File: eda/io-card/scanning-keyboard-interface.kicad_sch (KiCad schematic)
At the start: 17 parts, among them J7 Keyboard connector, U10 74HCT193, U11 74HCT541, U4 NE555P, U5 74HCT00, U8 74HCT138, U9 74HCT148

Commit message: Add expansion backplane
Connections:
- net Scancode0: now also U11.7 (A5); no longer U11.2 (A0)
- net Scancode1: now also U11.6 (A4); no longer U11.3 (A1)
- net Scancode2: now also U11.5 (A3); no longer U11.4 (A2)
- net Scancode3: now also U11.2 (A0); no longer U11.5 (A3)
- net Scancode4: now also U11.3 (A1); no longer U11.6 (A4)
- net Scancode5: now also U11.4 (A2); no longer U11.7 (A5)
- net mod0: now also U11.9 (A7); no longer U11.8 (A6)
- net mod1: now also U11.8 (A6); no longer U11.9 (A7)
- net row4: now also U9.4 (I7); no longer U9.1 (I4)
- net row5: now also U9.3 (I6); no longer U9.2 (I5)
- net row6: now also U9.2 (I5); no longer U9.3 (I6)
- net row7: now also U9.1 (I4); no longer U9.4 (I7)
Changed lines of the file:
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@@
     (stroke (width 0) (type default))
   )
-  (label "KeyboardBit6" (at 248.92 60.96 0)
+  (label "KeyboardBit6" (at 248.92 60.96 0) (fields_autoplaced)
     (effects (font (size 1.27 1.27)) (justify left bottom))
   )
@@
     (effects (font (size 1.27 1.27)) (justify right bottom))
   )
-  (label "row5" (at 113.03 111.76 180) (fields_autoplaced)
+  (label "row5" (at 113.03 114.3 180) (fields_autoplaced)
     (effects (font (size 1.27 1.27)) (justify right bottom))
   )
@@
     (effects (font (size 1.27 1.27)) (justify left bottom))
   )
-  (label "Scancode2" (at 217.17 50.8 180) (fields_autoplaced)
+  (label "Scancode2" (at 217.17 53.34 180) (fields_autoplaced)
     (effects (font (size 1.27 1.27)) (justify right bottom))
   )
-  (label "KeyboardBit1" (at 248.92 48.26 0)
+  (label "KeyboardBit1" (at 248.92 48.26 0) (fields_autoplaced)
     (effects (font (size 1.27 1.27)) (justify left bottom))
   )
@@
     (effects (font (size 1.27 1.27)) (justify left bottom))
   )
-  (label "KeyboardBit2" (at 248.92 50.8 0)
+  (label "KeyboardBit2" (at 248.92 50.8 0) (fields_autoplaced)
     (effects (font (size 1.27 1.27)) (justify left bottom))
   )
@@
     (effects (font (size 1.27 1.27)) (justify right bottom))
   )
-  (label "Scancode5" (at 217.17 58.42 180) (fields_autoplaced)
+  (label "Scancode5" (at 217.17 50.8 180) (fields_autoplaced)
     (effects (font (size 1.27 1.27)) (justify right bottom))
   )
-  (label "row7" (at 113.03 116.84 180) (fields_autoplaced)
+  (label "row7" (at 113.03 109.22 180) (fields_autoplaced)
     (effects (font (size 1.27 1.27)) (justify right bottom))
   )
-  (label "KeyboardBit7" (at 248.92 63.5 0)
+  (label "KeyboardBit7" (at 248.92 63.5 0) (fields_autoplaced)
     (effects (font (size 1.27 1.27)) (justify left bottom))
   )
@@
     (effects (font (size 1.27 1.27)) (justify left bottom))
   )
-  (label "KeyboardBit3" (at 248.92 53.34 0)
+  (label "KeyboardBit3" (at 248.92 53.34 0) (fields_autoplaced)
     (effects (font (size 1.27 1.27)) (justify left bottom))
   )
@@
     (effects (font (size 1.27 1.27)) (justify left bottom))
   )
-  (label "mod1" (at 207.01 63.5 0) (fields_autoplaced)
+  (label "mod1" (at 207.01 60.96 0) (fields_autoplaced)
     (effects (font (size 1.27 1.27)) (justify left bottom))
   )
@@
     (effects (font (size 1.27 1.27)) (justify left bottom))
   )
-  (label "row4" (at 113.03 109.22 180) (fields_autoplaced)
+  (label "row4" (at 113.03 116.84 180) (fields_autoplaced)
     (effects (font (size 1.27 1.27)) (justify right bottom))
   )
@@
     (effects (font (size 1.27 1.27)) (justify left bottom))
   )
-  (label "Scancode1" (at 217.17 48.26 180) (fields_autoplaced)
+  (label "Scancode1" (at 217.17 55.88 180) (fields_autoplaced)
     (effects (font (size 1.27 1.27)) (justify right bottom))
   )
-  (label "Scancode0" (at 217.17 45.72 180) (fields_autoplaced)
+  (label "Scancode0" (at 217.17 58.42 180) (fields_autoplaced)
     (effects (font (size 1.27 1.27)) (justify right bottom))
   )
-  (label "KeyboardBit5" (at 248.92 58.42 0)
+  (label "KeyboardBit5" (at 248.92 58.42 0) (fields_autoplaced)
     (effects (font (size 1.27 1.27)) (justify left bottom))
   )
-  (label "Scancode4" (at 217.17 55.88 180) (fields_autoplaced)
+  (label "Scancode4" (at 217.17 48.26 180) (fields_autoplaced)
     (effects (font (size 1.27 1.27)) (justify right bottom))
   )
@@
     (effects (font (size 1.27 1.27)) (justify right bottom))
   )
-  (label "mod0" (at 207.01 60.96 0) (fields_autoplaced)
+  (label "mod0" (at 207.01 63.5 0) (fields_autoplaced)
     (effects (font (size 1.27 1.27)) (justify left bottom))
   )
@@
     (effects (font (size 1.27 1.27)) (justify left bottom))
   )
-  (label "row6" (at 113.03 114.3 180) (fields_autoplaced)
+  (label "row6" (at 113.03 111.76 180) (fields_autoplaced)
     (effects (font (size 1.27 1.27)) (justify right bottom))
   )
-  (label "Scancode3" (at 217.17 53.34 180) (fields_autoplaced)
+  (label "Scancode3" (at 217.17 45.72 180) (fields_autoplaced)
     (effects (font (size 1.27 1.27)) (justify right bottom))
   )
@@
     (effects (font (size 1.27 1.27)) (justify right bottom))
   )
-  (label "KeyboardBit4" (at 248.92 55.88 0)
+  (label "KeyboardBit4" (at 248.92 55.88 0) (fields_autoplaced)
     (effects (font (size 1.27 1.27)) (justify left bottom))
   )
-  (label "KeyboardBit0" (at 248.92 45.72 0)
+  (label "KeyboardBit0" (at 248.92 45.72 0) (fields_autoplaced)
     (effects (font (size 1.27 1.27)) (justify left bottom))
   )

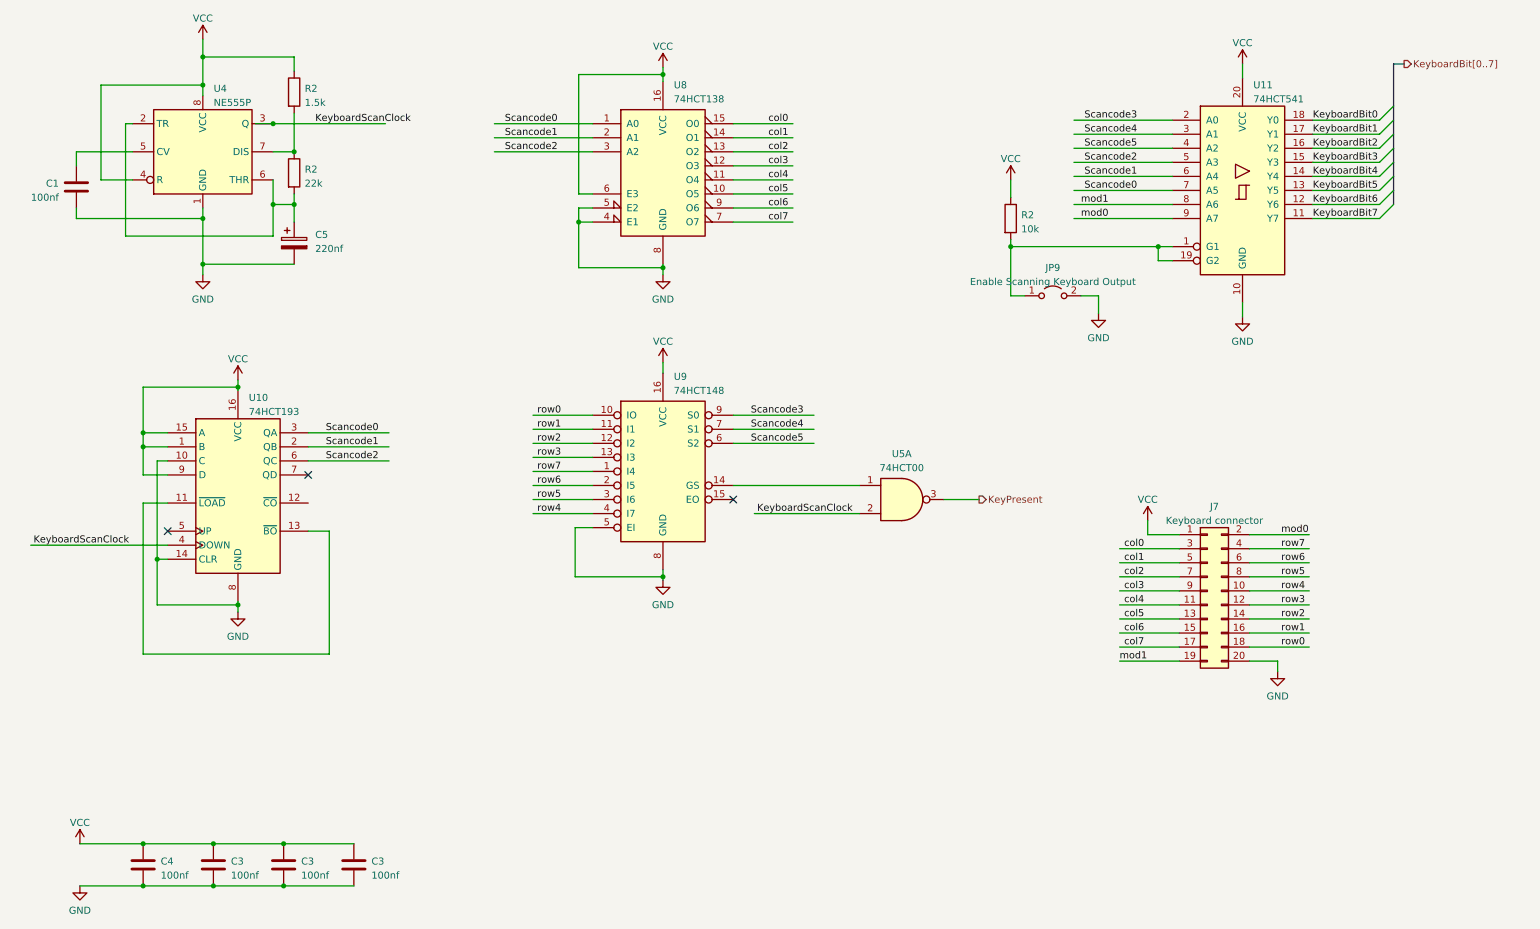
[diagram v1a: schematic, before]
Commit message: EDA work for new expansion header
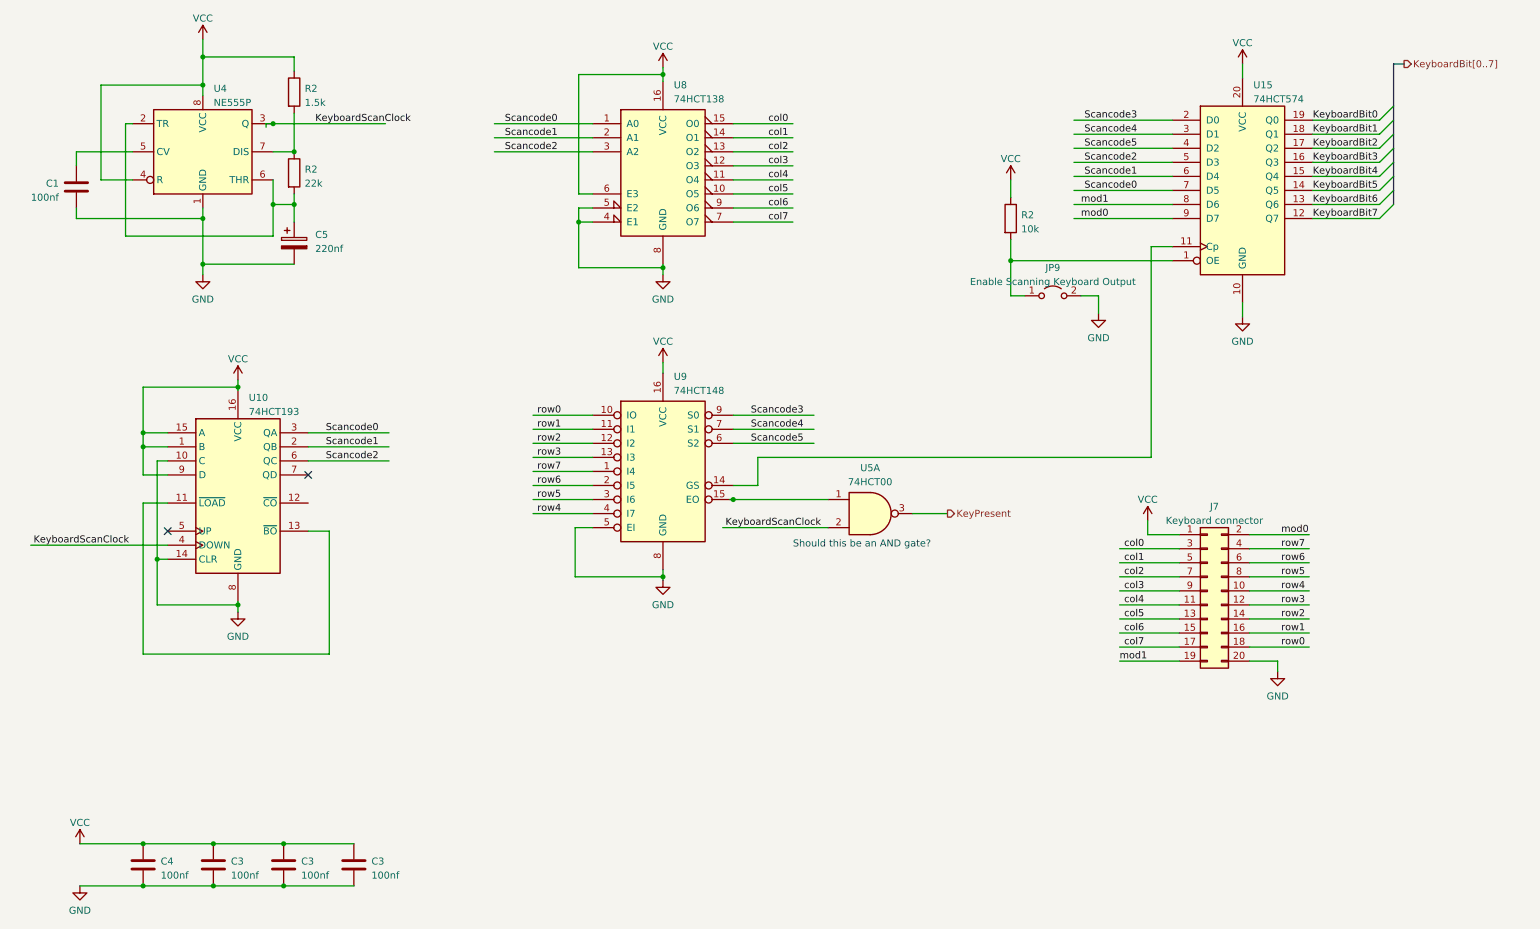
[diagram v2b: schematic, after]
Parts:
- removed U11: 74HCT541, Package_DIP:DIP-20_W7.62mm, symbol 74xx:74HCT541
- added U15: 74HCT574, Package_DIP:DIP-20_W7.62mm, symbol 74xx:74HCT574
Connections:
- net GND: now also U15.10 (GND)
- net KeyboardBit0: now also U15.19 (Q0)
- net KeyboardBit1: now also U15.18 (Q1)
- net KeyboardBit2: now also U15.17 (Q2)
- net KeyboardBit3: now also U15.16 (Q3)
- net KeyboardBit4: now also U15.15 (Q4)
- net KeyboardBit5: now also U15.14 (Q5)
- net KeyboardBit6: now also U15.13 (Q6)
- net KeyboardBit7: now also U15.12 (Q7)
- net Scancode0: now also U15.7 (D5)
- net Scancode1: now also U15.6 (D4)
- net Scancode2: now also U15.5 (D3)
- net Scancode3: now also U15.2 (D0)
- net Scancode4: now also U15.3 (D1)
- net Scancode5: now also U15.4 (D2)
- net VCC: now also U15.20 (VCC)
- net mod0: now also U15.9 (D7)
- net mod1: now also U15.8 (D6)
- net at JP9.1 (A), R2.2: now also U15.1 (OE)
- net at U9.14 (GS): now also U15.11 (Cp); no longer U5.1
- net at U9.15 (EO): now also U5.1
- no-connect marks 3 -> 2
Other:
- note added: "Should this be an AND gate?"
- moved on the sheet: U5A

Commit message: Normalize cap size
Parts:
- C1, C3, C4: footprint Capacitor_THT:C_Disc_D3.4mm_W2.1mm_P2.50mm -> Capacitor_THT:C_Disc_D3.8mm_W2.6mm_P2.50mm
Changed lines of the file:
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@@
       (effects (font (size 1.27 1.27)) (justify left))
     )
-    (property "Footprint" "Capacitor_THT:C_Disc_D3.4mm_W2.1mm_P2.50mm" (at 38.4302 184.15 0)
+    (property "Footprint" "Capacitor_THT:C_Disc_D3.8mm_W2.6mm_P2.50mm" (at 38.4302 184.15 0)
       (effects (font (size 1.27 1.27)) hide)
     )
@@
       (effects (font (size 1.27 1.27)) (justify left))
     )
-    (property "Footprint" "Capacitor_THT:C_Disc_D3.4mm_W2.1mm_P2.50mm" (at 76.5302 184.15 0)
+    (property "Footprint" "Capacitor_THT:C_Disc_D3.8mm_W2.6mm_P2.50mm" (at 76.5302 184.15 0)
       (effects (font (size 1.27 1.27)) hide)
     )
@@
       (effects (font (size 1.27 1.27)) (justify left))
     )
-    (property "Footprint" "Capacitor_THT:C_Disc_D3.4mm_W2.1mm_P2.50mm" (at 24.4348 61.595 0)
+    (property "Footprint" "Capacitor_THT:C_Disc_D3.8mm_W2.6mm_P2.50mm" (at 24.4348 61.595 0)
       (effects (font (size 1.27 1.27)) hide)
     )
@@
       (effects (font (size 1.27 1.27)) (justify left))
     )
-    (property "Footprint" "Capacitor_THT:C_Disc_D3.4mm_W2.1mm_P2.50mm" (at 63.8302 184.15 0)
+    (property "Footprint" "Capacitor_THT:C_Disc_D3.8mm_W2.6mm_P2.50mm" (at 63.8302 184.15 0)
       (effects (font (size 1.27 1.27)) hide)
     )
@@
       (effects (font (size 1.27 1.27)) (justify left))
     )
-    (property "Footprint" "Capacitor_THT:C_Disc_D3.4mm_W2.1mm_P2.50mm" (at 51.1302 184.15 0)
-      (effects (font (size 1.27 1.27)) hide)
-    )
+    (property "Footprint" "Capacitor_THT:C_Disc_D3.8mm_W2.6mm_P2.50mm" (at 51.1302 184.15 0)
+      (effects (font (size 1.27 1.27)) hide)
+    )

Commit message: Rerouting IO card
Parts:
- J7: footprint Connector_PinSocket_2.54mm:PinSocket_2x10_P2.54mm_Vertical -> Connector_PinHeader_2.54mm:PinHeader_2x10_P2.54mm_Horizontal
- renumbered C3 to C10, C1 to C6, C4 to C7, C3 to C8, C3 to C9, JP9 to JP10, R2 to R3, R2 to R4, R2 to R5

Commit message: Add SPI
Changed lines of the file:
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@@
 (kicad_sch
-	(version 20231120)
+	(version 20250114)
 	(generator "eeschema")
-	(generator_version "8.0")
+	(generator_version "9.0")
 	(paper "A4")
+	(text "Should this be an AND gate?"
+		(exclude_from_sim no)
+		(at 154.94 123.19 0)
+		(effects
+			(font
+				(size 1.27 1.27)
+			)
+			(justify left bottom)
+		)
+	)
 	(junction
 		(at 144.145 114.3)
@@
 		)
 	)
-	(text "Should this be an AND gate?"
-		(exclude_from_sim no)
-		(at 154.94 123.19 0)
-		(effects
-			(font
-				(size 1.27 1.27)
-			)
-			(justify left bottom)
-		)
-	)
 	(label "KeyboardBit6"
 		(at 248.92 60.96 0)
-		(fields_autoplaced yes)
 		(effects
 			(font
@@
 	(label "row4"
 		(at 243.205 130.81 0)
-		(fields_autoplaced yes)
 		(effects
 			(font
@@
 	(label "col0"
 		(at 150.495 46.355 0)
-		(fields_autoplaced yes)
 		(effects
 			(font
@@
 	(label "row3"
 		(at 113.03 106.68 180)
-		(fields_autoplaced yes)
 		(effects
 			(font
@@
 	(label "col7"
 		(at 150.495 64.135 0)
-		(fields_autoplaced yes)
 		(effects
 			(font
@@
 	(label "col3"
 		(at 218.44 130.81 180)
-		(fields_autoplaced yes)
 		(effects
 			(font
@@
 	(label "row5"
 		(at 113.03 114.3 180)
-		(fields_autoplaced yes)
 		(effects
 			(font
@@
 	(label "col5"
 		(at 150.495 59.055 0)
-		(fields_autoplaced yes)
 		(effects
 			(font
@@
 	(label "col3"
 		(at 150.495 53.975 0)
-		(fields_autoplaced yes)
 		(effects
 			(font
@@
 	(label "Scancode2"
 		(at 70.485 107.315 0)
-		(fields_autoplaced yes)
 		(effects
 			(font
@@
 	(label "Scancode2"
 		(at 217.17 53.34 180)
-		(fields_autoplaced yes)
 		(effects
 			(font
@@
 	(label "KeyboardBit1"
 		(at 248.92 48.26 0)
-		(fields_autoplaced yes)
 		(effects
 			(font
@@
 	(label "KeyboardScanClock"
 		(at 34.925 122.555 180)
-		(fields_autoplaced yes)
 		(effects
 			(font
@@
 	(label "Scancode0"
 		(at 70.485 102.235 0)
-		(fields_autoplaced yes)
 		(effects
 			(font
@@
 	(label "Scancode1"
 		(at 70.485 104.775 0)
-		(fields_autoplaced yes)
 		(effects
 			(font
@@
 	(label "KeyboardBit2"
 		(at 248.92 50.8 0)
-		(fields_autoplaced yes)
 		(effects
 			(font
@@
 	(label "row1"
 		(at 113.03 101.6 180)
-		(fields_autoplaced yes)
 		(effects
 			(font
@@
 	(label "Scancode5"
 		(at 217.17 50.8 180)
-		(fields_autoplaced yes)
 		(effects
 			(font
@@
 	(label "row7"
 		(at 113.03 109.22 180)
-		(fields_autoplaced yes)
 		(effects
 			(font
@@
 	(label "KeyboardBit7"
 		(at 248.92 63.5 0)
-		(fields_autoplaced yes)
 		(effects
 			(font
@@
 	(label "row6"
 		(at 243.205 125.73 0)
-		(fields_autoplaced yes)
 		(effects
 			(font
@@
 	(label "KeyboardBit3"
 		(at 248.92 53.34 0)
-		(fields_autoplaced yes)
 		(effects
 			(font
@@
 	(label "col2"
 		(at 150.495 51.435 0)
-		(fields_autoplaced yes)
 		(effects
 			(font
@@
 	(label "row1"
 		(at 243.205 138.43 0)
-		(fields_autoplaced yes)
 		(effects
 			(font
@@
 	(label "mod1"
 		(at 207.01 60.96 0)
-		(fields_autoplaced yes)
 		(effects
 			(font
@@
 	(label "col4"
 		(at 150.495 56.515 0)
-		(fields_autoplaced yes)
 		(effects
 			(font
@@
 	(label "row4"
 		(at 113.03 116.84 180)
-		(fields_autoplaced yes)
 		(effects
 			(font
@@
 	(label "col1"
 		(at 218.44 125.73 180)
-		(fields_autoplaced yes)
 		(effects
 			(font
@@
 	(label "col6"
 		(at 218.44 138.43 180)
-		(fields_autoplaced yes)
 		(effects
 			(font
@@
 	(label "row2"
 		(at 243.205 135.89 0)
-		(fields_autoplaced yes)
 		(effects
 			(font
@@
 	(label "KeyboardScanClock"
 		(at 160.02 119.38 180)
-		(fields_autoplaced yes)
 		(effects
 			(font
@@
 	(label "col7"
 		(at 218.44 140.97 180)
-		(fields_autoplaced yes)
 		(effects
 			(font
@@
 	(label "row5"
 		(at 243.205 128.27 0)
-		(fields_autoplaced yes)
 		(effects
 			(font
@@
 	(label "KeyboardScanClock"
 		(at 68.58 46.355 0)
-		(fields_autoplaced yes)
 		(effects
 			(font
@@
 	(label "row3"
 		(at 243.205 133.35 0)
-		(fields_autoplaced yes)
 		(effects
 			(font
@@
 	(label "Scancode1"
 		(at 217.17 55.88 180)
-		(fields_autoplaced yes)
 		(effects
 			(font
@@
 	(label "Scancode0"
 		(at 217.17 58.42 180)
-		(fields_autoplaced yes)
 		(effects
 			(font
@@
 	(label "KeyboardBit5"
 		(at 248.92 58.42 0)
-		(fields_autoplaced yes)
 		(effects
 			(font
@@
 	(label "Scancode4"
 		(at 217.17 48.26 180)
-		(fields_autoplaced yes)
 		(effects
 			(font
@@
 	(label "row0"
 		(at 113.03 99.06 180)
-		(fields_autoplaced yes)
 		(effects
 			(font
@@
 	(label "col4"
 		(at 218.44 133.35 180)
-		(fields_autoplaced yes)
 		(effects
 			(font
@@
 	(label "col1"
 		(at 150.495 48.895 0)
-		(fields_autoplaced yes)
 		(effects
 			(font
@@
 	(label "Scancode5"
 		(at 147.32 104.14 0)
-		(fields_autoplaced yes)
 		(effects
 			(font
@@
 	(label "mod0"
 		(at 243.205 120.65 0)
-		(fields_autoplaced yes)
 		(effects
 			(font
@@
 	(label "Scancode0"
 		(at 112.395 46.355 180)
-		(fields_autoplaced yes)
 		(effects
 			(font
@@
 	(label "Scancode2"
 		(at 112.395 51.435 180)
-		(fields_autoplaced yes)
 		(effects
 			(font
@@
 	(label "Scancode4"
 		(at 147.32 101.6 0)
-		(fields_autoplaced yes)
 		(effects
 			(font
@@
 	(label "row0"
 		(at 243.205 140.97 0)
-		(fields_autoplaced yes)
 		(effects
 			(font
@@
 	(label "mod1"
 		(at 213.995 143.51 0)
-		(fields_autoplaced yes)
 		(effects
 			(font
@@
 	(label "col6"
 		(at 150.495 61.595 0)
-		(fields_autoplaced yes)
 		(effects
 			(font
@@
 	(label "row2"
 		(at 113.03 104.14 180)
-		(fields_autoplaced yes)
 		(effects
 			(font
@@
 	(label "col0"
 		(at 218.44 123.19 180)
-		(fields_autoplaced yes)
 		(effects
 			(font
@@
 	(label "mod0"
 		(at 207.01 63.5 0)
-		(fields_autoplaced yes)
 		(effects
 			(font
@@
 	(label "Scancode3"
 		(at 147.32 99.06 0)
-		(fields_autoplaced yes)
 		(effects
 			(font
@@
 	(label "row6"
 		(at 113.03 111.76 180)
-		(fields_autoplaced yes)
 		(effects
 			(font
@@
 	(label "Scancode3"
 		(at 217.17 45.72 180)
-		(fields_autoplaced yes)
 		(effects
 			(font
@@
 	(label "row7"
 		(at 243.205 123.19 0)
-		(fields_autoplaced yes)
 		(effects
 			(font
@@
 	(label "Scancode1"
 		(at 112.395 48.895 180)
-		(fields_autoplaced yes)
 		(effects
 			(font
@@
 	(label "col2"
 		(at 218.44 128.27 180)
-		(fields_autoplaced yes)
 		(effects
 			(font
@@
 	(label "col5"
 		(at 218.44 135.89 180)
-		(fields_autoplaced yes)
 		(effects
 			(font
@@
 	(label "KeyboardBit4"
 		(at 248.92 55.88 0)
-		(fields_autoplaced yes)
 		(effects
 			(font
@@
 	(label "KeyboardBit0"
 		(at 248.92 45.72 0)
-		(fields_autoplaced yes)
 		(effects
 			(font
@@
 		(shape output)
 		(at 265.43 35.56 0)
-		(fields_autoplaced yes)
 		(effects
 			(font
@@
 		(shape output)
 		(at 182.88 116.84 0)
-		(fields_autoplaced yes)
-		(effects
-			(font
+		(effects
+			(font
